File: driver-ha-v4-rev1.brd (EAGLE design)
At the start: 22 x 40.6 mm, 14 parts, among them J1 1X2-3.5MM, J2 1X2-3.5MM, K2 M3XXH

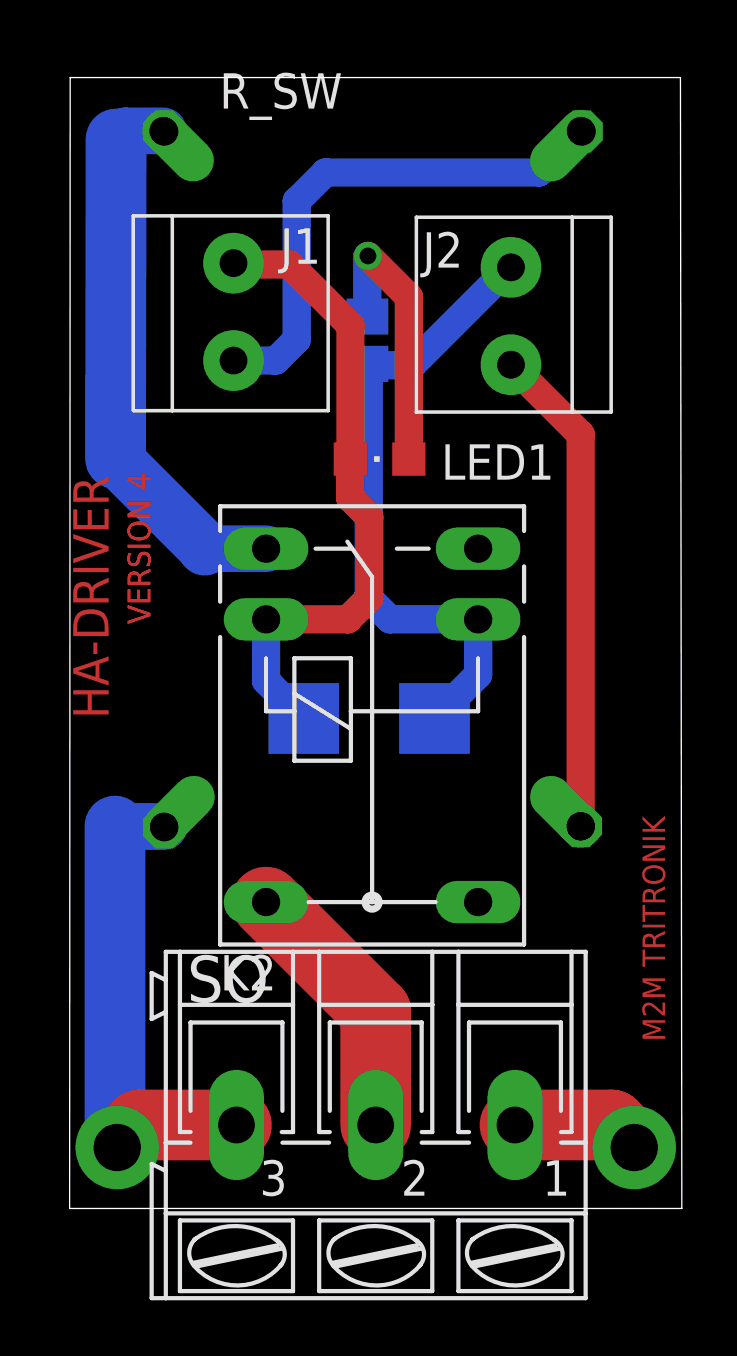
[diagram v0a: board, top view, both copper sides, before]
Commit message: Tiding up and add a new ha-driver
revised the ha-driver to 1-layer PCB
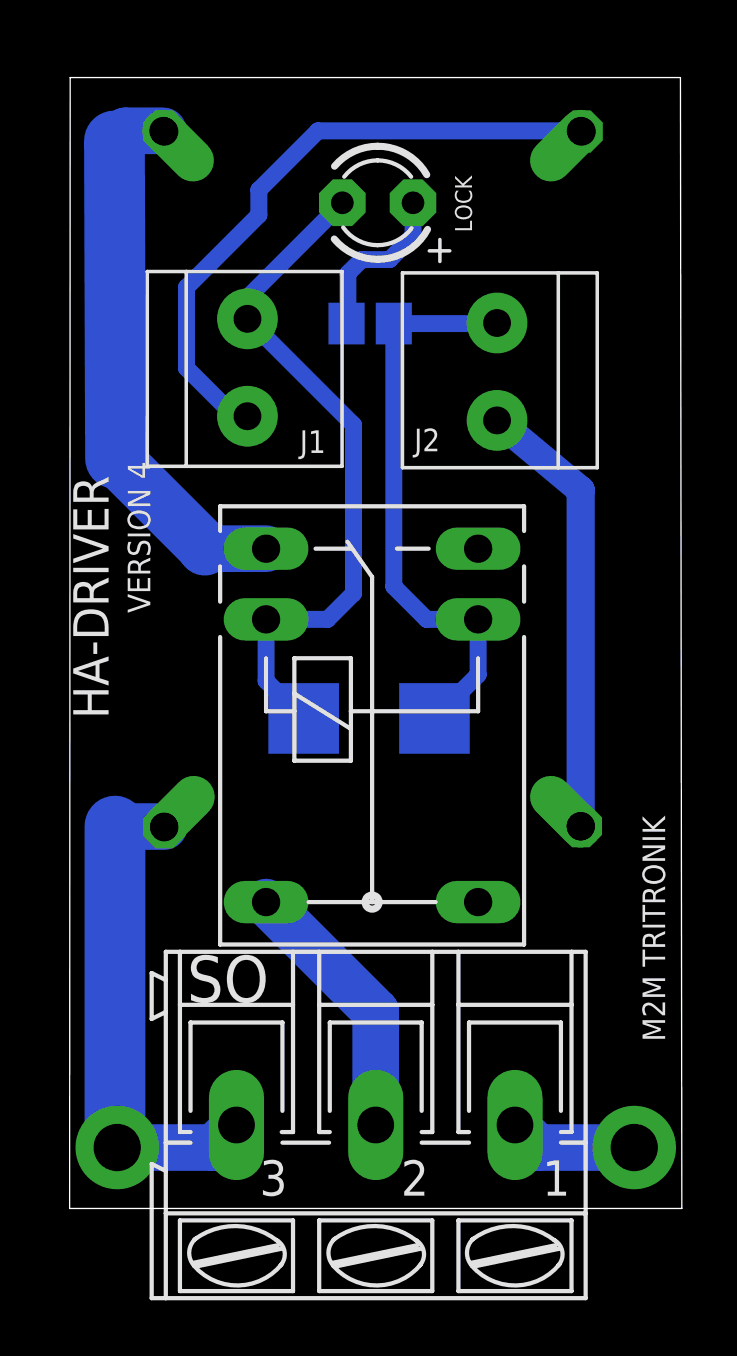
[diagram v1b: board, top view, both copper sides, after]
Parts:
- removed LED1: (no value), adafruit:CHIPLED_0805
- added LOCK: (no value), adafruit:LED3MM
- moved J1 2.06 mm to (6.39, 30.3)
- moved J2 2.06 mm to (15.4, 30.0)
- moved R1 0.61 mm to (10.8, 31.8), turned to 180 degrees
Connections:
- net I_DRIVE: now also LOCK.K; no longer LED1.C
- net N$2: now also LOCK.A; no longer LED1.A
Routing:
- net N$2: track 10.1 -> 5.92 mm, vias 1 -> 0
- net IN_SWITCH: track 18.8 -> 22.8 mm
- net VCC: track 23.5 -> 20.9 mm
- net GND: track 17.6 -> 16.0 mm
- net I_DRIVE: track 23.7 -> 24.7 mm
